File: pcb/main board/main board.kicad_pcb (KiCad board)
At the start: 2 copper layers, 115 x 160.5 mm, 83 parts, among them J1 Motor 0 Conn, J10 12V Battery, J11 BAU, J12 Servo 4 Conn, J13 Servo 1 Conn, J14 Servo 2 Conn, J15 Servo 3 Conn, J16 Servo 5 Conn, J17 Servo 6 Conn, J18 Servo 7 Conn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

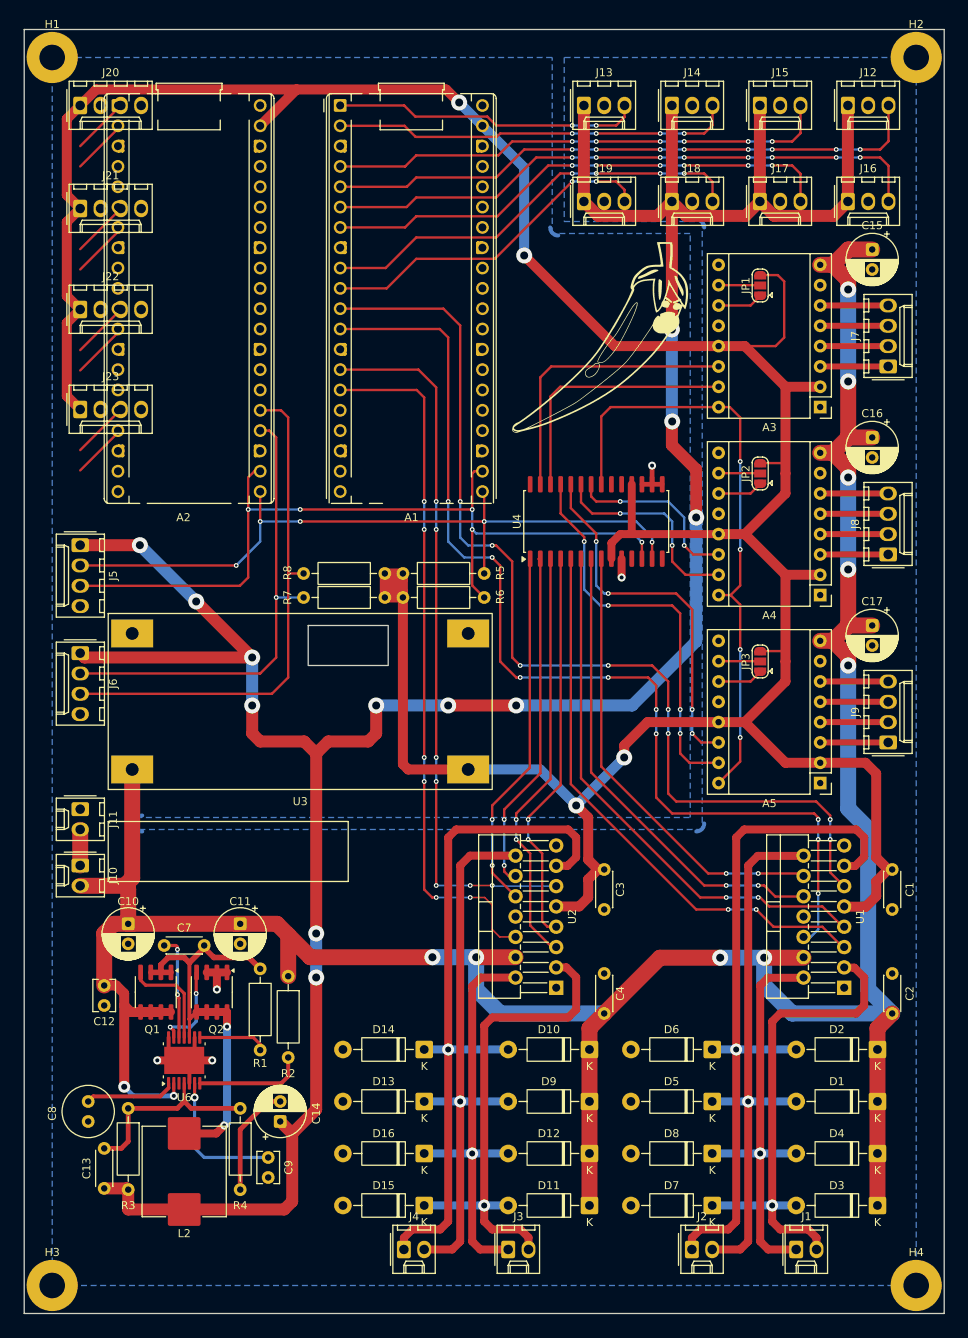
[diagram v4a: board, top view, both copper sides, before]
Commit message: Finished adding holes and connectors
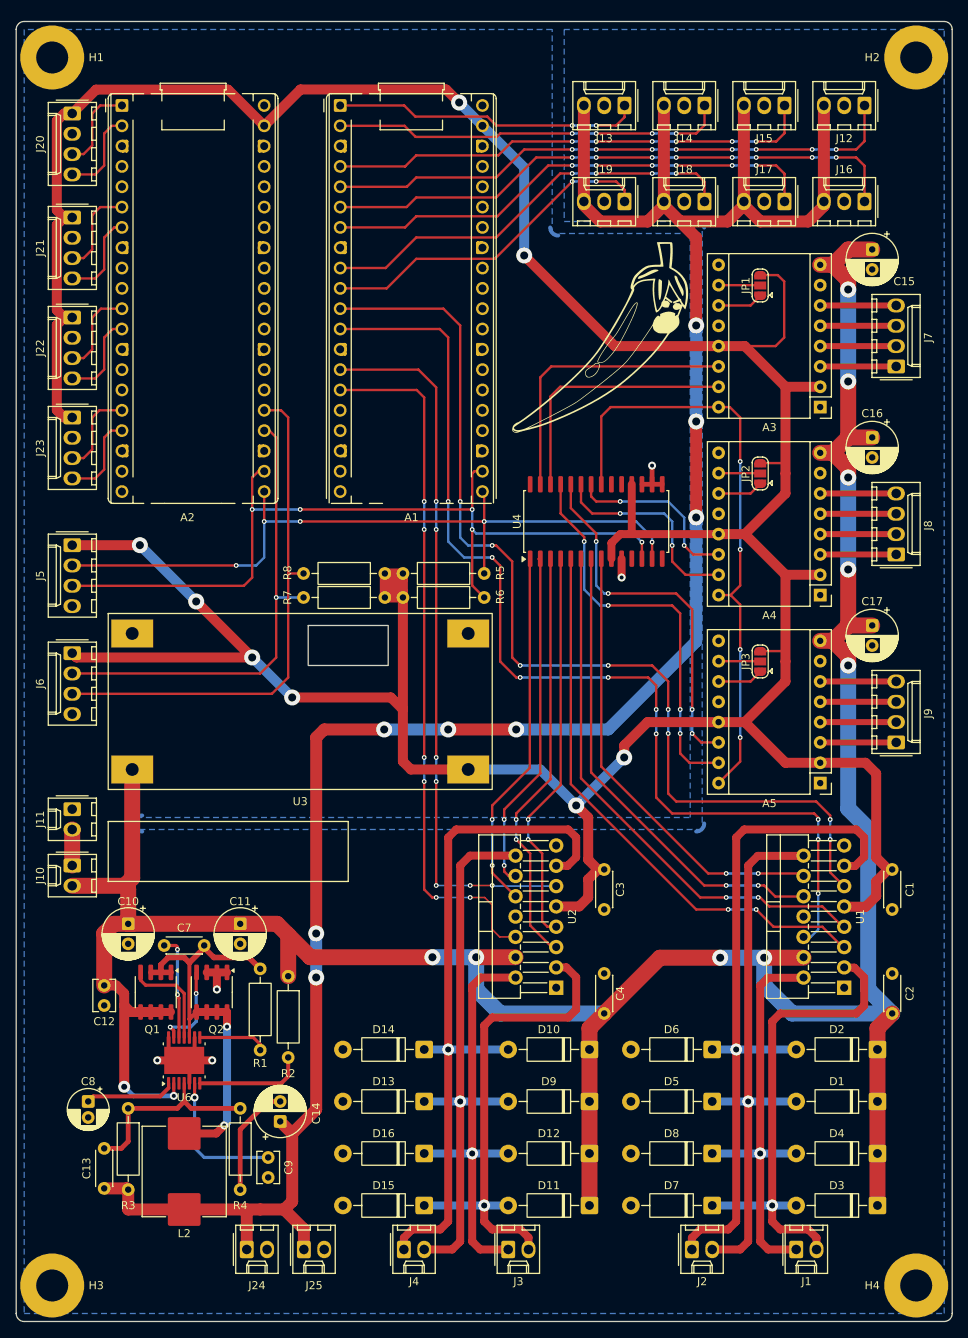
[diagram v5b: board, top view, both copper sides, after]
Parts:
- added J24: Fan 1 Conn, Connector_Molex:Molex_KK-254_AE-6410-02A_1x02_P2.54mm_Vertical, F.Cu at (202.8, 217.0)
- added J25: Fan 2 Conn, Connector_Molex:Molex_KK-254_AE-6410-02A_1x02_P2.54mm_Vertical, F.Cu at (210.0, 217.0)
- C8: footprint Capacitor_THT:C_Radial_D6.3mm_H5.0mm_P2.50mm -> Capacitor_THT:CP_Radial_D5.0mm_P2.00mm
- H1, H2, H3, H4: footprint MountingHole:MountingHole_3.2mm_M3_Pad -> MountingHole:MountingHole_4mm_Pad
- moved J13 5.08 mm to (250.0, 74.0), turned to 180 degrees
- moved J19 5.08 mm to (250.0, 86.0), turned to 180 degrees
- moved J18 4.08 mm to (260.0, 86.0), turned to 180 degrees
- moved J14 4.08 mm to (260.0, 74.0), turned to 180 degrees
- moved J15 3.08 mm to (270.0, 74.0), turned to 180 degrees
- moved J17 3.08 mm to (270.0, 86.0), turned to 180 degrees
- moved J12 2.08 mm to (280.0, 74.0), turned to 180 degrees
- moved J16 2.08 mm to (280.0, 86.0), turned to 180 degrees
- moved J21 1.50 mm to (181.0, 88.0), turned to -90 degrees
- moved J20 1.41 mm to (181.0, 75.0), turned to -90 degrees
- moved J22 1.41 mm to (181.0, 100.5), turned to -90 degrees
- moved J23 1.41 mm to (181.0, 113.0), turned to -90 degrees
- moved J10 1.00 mm to (181.0, 169.0)
- moved J11 1.00 mm to (181.0, 162.0)
- moved J5 1.00 mm to (181.0, 129.0)
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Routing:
- net +5VL: track 412.2 -> 485.4 mm, vias 4 -> 8
- net +5VP: track 350.6 -> 290.1 mm, vias 12 -> 8
- net Codeur 2 Pin 1: track 7.22 -> 11.4 mm
- net Codeur 4 Pin 2: track 6.94 -> 11.0 mm
- net Codeur 4 Pin 1: track 6.94 -> 11.0 mm
- net Codeur 1 Pin 2: track 7.04 -> 11.1 mm
- net Codeur 1 Pin 1: track 7.04 -> 11.1 mm
- net Codeur 2 Pin 2: track 7.22 -> 11.2 mm
- net Codeur 3 Pin 1: track 7.14 -> 11.1 mm
- net Codeur 3 Pin 2: track 7.14 -> 11.1 mm
- net Servo 5 PWM: track 76.0 -> 73.0 mm
- net Servo 4 PWM: track 75.4 -> 72.4 mm
- net I2C 0 SDA: track 92.8 -> 95.0 mm
- net Servo 6 PWM: track 64.6 -> 62.6 mm
- net Servo 3 PWM: track 62.7 -> 60.7 mm
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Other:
- board size 115 x 160.5 mm -> 117 x 162.5 mm

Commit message: Updated PCB and corrected errors
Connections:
- C14 pad 2: Net-(C14-Pad2) -> GNDPWR
- R4 pad 2: Net-(C14-Pad2) -> GNDPWR
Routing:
- net Net-(C14-Pad2): track 14.0 -> 0.00 mm
- net GNDPWR: track 46.4 -> 60.4 mm
